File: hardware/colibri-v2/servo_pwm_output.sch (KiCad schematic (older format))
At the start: 20 parts

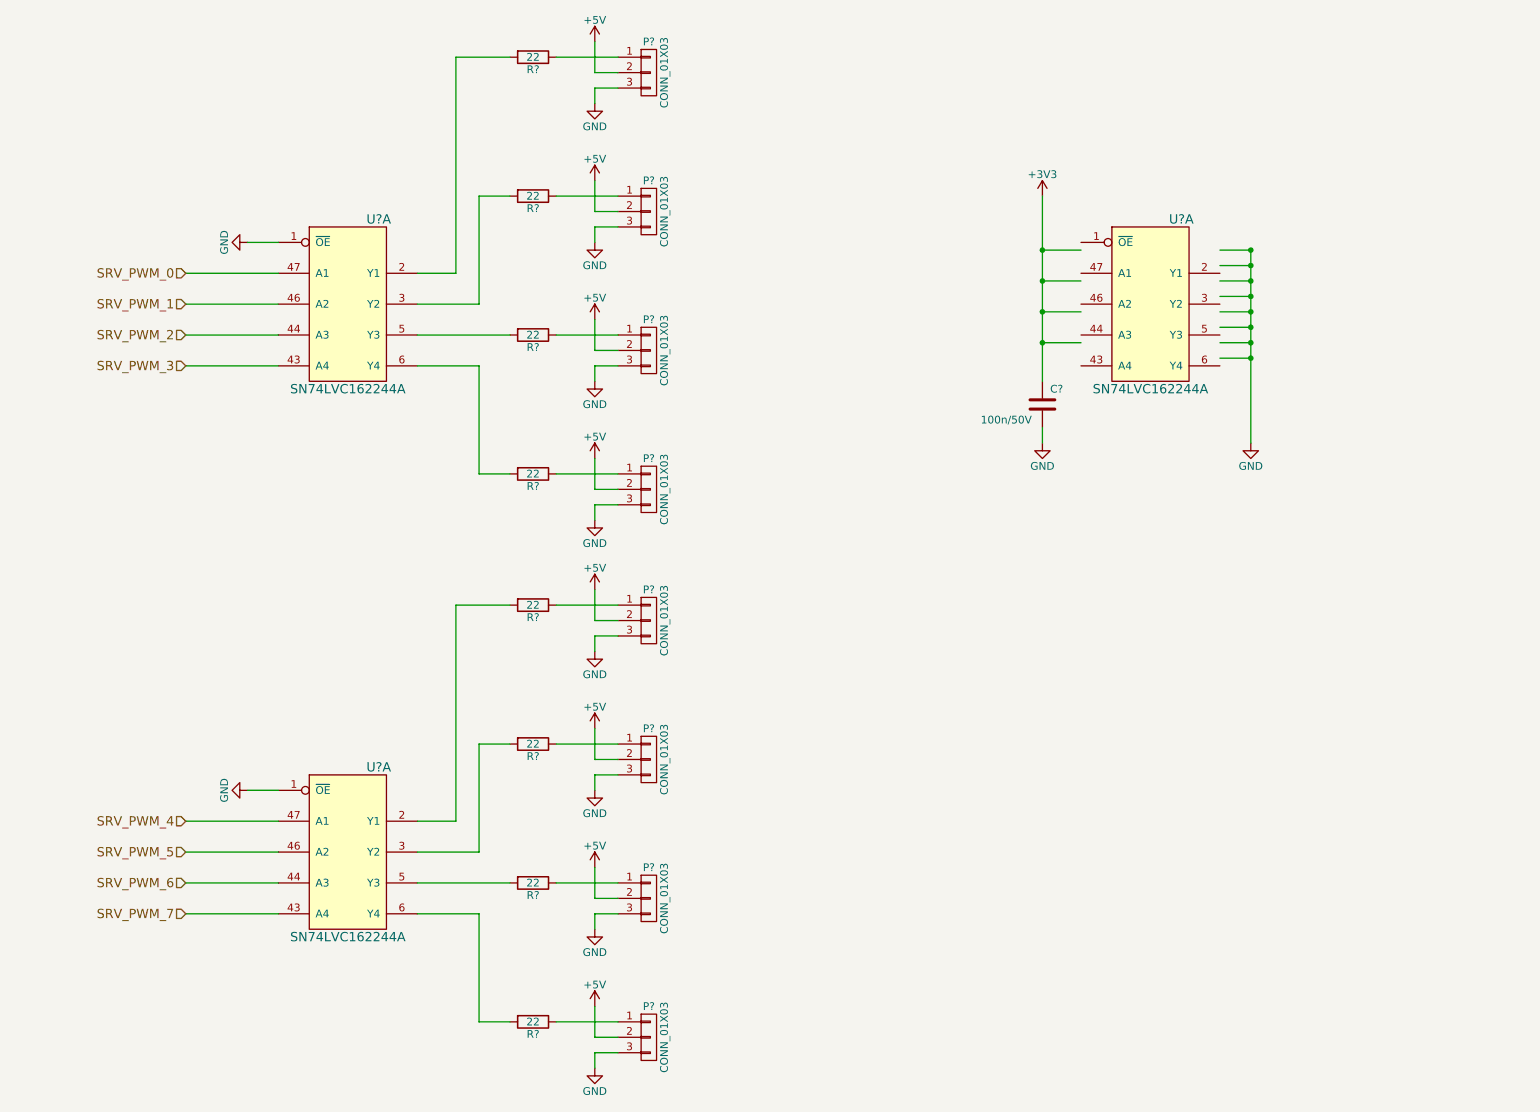
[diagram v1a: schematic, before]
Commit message: Work on wandboard lcd and usb
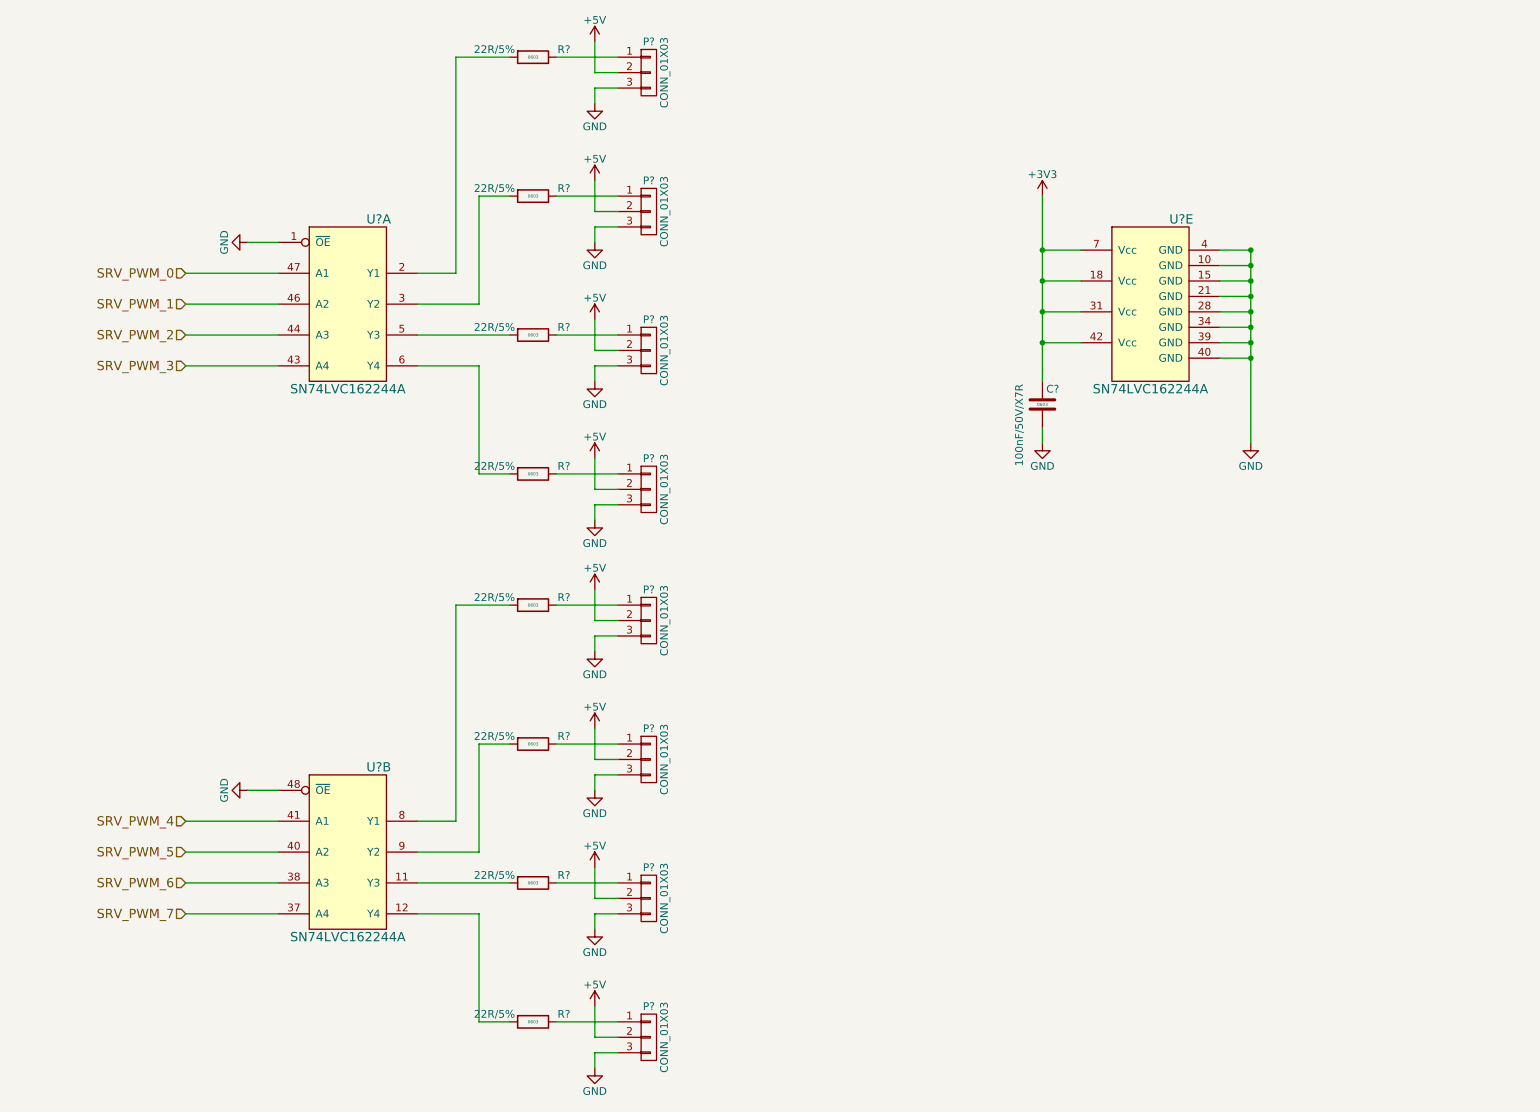
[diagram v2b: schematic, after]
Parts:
- removed C?: 100n/50V, symbol C
- removed R? (x8): 22, Resistors_SMD:R_0603, symbol R
- added C?: 100nF/50V/X7R, Capacitors_SMD:C_0603, symbol C_SMT
- added R? (x8): 22R/5%, Resistors_SMD:R_0603, symbol R_SMT
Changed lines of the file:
@@
 	1    0    0    -1
-$EndComp
-$Comp
-L R R?
-U 1 1 5619166B
-P 4300 4450
-F 0 "R?" V 4380 4450 50  0000 C CNN
-F 1 "22" V 4300 4450 50  0000 C CNN
-F 2 "Resistors_SMD:R_0603" V 4230 4450 30  0001 C CNN
-F 3 "" H 4300 4450 30  0000 C CNN
-	1    4300 4450
-	0    1    1    0
 $EndComp
 Text HLabel 2050 5850 0    60   Input ~ 0
@@
 	1    0    0    -1
 $EndComp
-$Comp
-L R R?
-U 1 1 56191934
-P 4300 5350
-F 0 "R?" V 4380 5350 50  0000 C CNN
-F 1 "22" V 4300 5350 50  0000 C CNN
-F 2 "Resistors_SMD:R_0603" V 4230 5350 30  0001 C CNN
-F 3 "" H 4300 5350 30  0000 C CNN
-	1    4300 5350
-	0    1    1    0
-$EndComp
 Text HLabel 2050 6050 0    60   Input ~ 0
 SRV_PWM_5
@@
 	1    0    0    -1
 $EndComp
-$Comp
-L R R?
-U 1 1 56191B34
-P 4300 6250
-F 0 "R?" V 4380 6250 50  0000 C CNN
-F 1 "22" V 4300 6250 50  0000 C CNN
-F 2 "Resistors_SMD:R_0603" V 4230 6250 30  0001 C CNN
-F 3 "" H 4300 6250 30  0000 C CNN
-	1    4300 6250
-	0    1    1    0
-$EndComp
 Text HLabel 2050 6250 0    60   Input ~ 0
 SRV_PWM_6
@@
 	1    0    0    -1
 $EndComp
-$Comp
-L R R?
-U 1 1 56191CF8
-P 4300 7150
-F 0 "R?" V 4380 7150 50  0000 C CNN
-F 1 "22" V 4300 7150 50  0000 C CNN
-F 2 "Resistors_SMD:R_0603" V 4230 7150 30  0001 C CNN
-F 3 "" H 4300 7150 30  0000 C CNN
-	1    4300 7150
-	0    1    1    0
-$EndComp
 Text HLabel 2050 6450 0    60   Input ~ 0
 SRV_PWM_7
@@
 	1    0    0    -1
 $EndComp
-$Comp
-L R R?
-U 1 1 5619340F
-P 4300 900
-F 0 "R?" V 4380 900 50  0000 C CNN
-F 1 "22" V 4300 900 50  0000 C CNN
-F 2 "Resistors_SMD:R_0603" V 4230 900 30  0001 C CNN
-F 3 "" H 4300 900 30  0000 C CNN
-	1    4300 900
-	0    1    1    0
-$EndComp
 Text HLabel 2050 2300 0    60   Input ~ 0
 SRV_PWM_0
@@
 	1    0    0    -1
 $EndComp
-$Comp
-L R R?
-U 1 1 56193435
-P 4300 1800
-F 0 "R?" V 4380 1800 50  0000 C CNN
-F 1 "22" V 4300 1800 50  0000 C CNN
-F 2 "Resistors_SMD:R_0603" V 4230 1800 30  0001 C CNN
-F 3 "" H 4300 1800 30  0000 C CNN
-	1    4300 1800
-	0    1    1    0
-$EndComp
 Text HLabel 2050 2500 0    60   Input ~ 0
 SRV_PWM_1
@@
 	1    0    0    -1
 $EndComp
-$Comp
-L R R?
-U 1 1 5619345B
-P 4300 2700
-F 0 "R?" V 4380 2700 50  0000 C CNN
-F 1 "22" V 4300 2700 50  0000 C CNN
-F 2 "Resistors_SMD:R_0603" V 4230 2700 30  0001 C CNN
-F 3 "" H 4300 2700 30  0000 C CNN
-	1    4300 2700
-	0    1    1    0
-$EndComp
 Text HLabel 2050 2700 0    60   Input ~ 0
 SRV_PWM_2
@@
 	1    0    0    -1
 $EndComp
-$Comp
-L R R?
-U 1 1 56193481
-P 4300 3600
-F 0 "R?" V 4380 3600 50  0000 C CNN
-F 1 "22" V 4300 3600 50  0000 C CNN
-F 2 "Resistors_SMD:R_0603" V 4230 3600 30  0001 C CNN
-F 3 "" H 4300 3600 30  0000 C CNN
-	1    4300 3600
-	0    1    1    0
-$EndComp
 Text HLabel 2050 2900 0    60   Input ~ 0
 SRV_PWM_3
@@
 $EndComp
 $Comp
-L C C?
-U 1 1 5619436E
-P 7600 3150
-F 0 "C?" H 7650 3250 50  0000 L CNN
-F 1 "100n/50V" H 7200 3050 50  0000 L CNN
-F 2 "" H 7638 3000 30  0001 C CNN
-F 3 "" H 7600 3150 60  0000 C CNN
-	1    7600 3150
-	1    0    0    -1
-$EndComp
-$Comp
 L SN74LVC162244A U?
 U 1 1 56245EEA
@@
 $Comp
 L SN74LVC162244A U?
-U 1 1 5624684B
+U 2 1 5624684B
 P 3100 6050
 F 0 "U?" H 3300 6600 60  0000 C CNN
@@
 F 2 "" H 3100 5900 60  0001 C CNN
 F 3 "" H 3100 5900 60  0000 C CNN
-	1    3100 6050
+	2    3100 6050
 	1    0    0    -1
 $EndComp
 $Comp
 L SN74LVC162244A U?
-U 1 1 562469AD
+U 5 1 562469AD
 P 8300 2500
 F 0 "U?" H 8500 3050 60  0000 C CNN
@@
 F 2 "" H 8300 2350 60  0001 C CNN
 F 3 "" H 8300 2350 60  0000 C CNN
-	1    8300 2500
+	5    8300 2500
 	1    0    0    -1
 $EndComp
@@
 Wire Wire Line
 	2450 2100 2650 2100
+$Comp
+L R_SMT R?
+U 1 1 5633B5FF
+P 4300 900
+F 0 "R?" V 4250 1100 50  0000 C CNN
+F 1 "22R/5%" V 4250 650 50  0000 C CNN
+F 2 "Resistors_SMD:R_0603" V 4450 900 30  0001 C CNN
+F 3 "" V 4380 900 30  0000 C CNN
+F 4 "0603" V 4300 900 20  0000 C CNN "SMT"
+F 5 "9331891" V 4500 900 30  0001 C CNN "Part"
+F 6 "Farnell" V 4550 900 30  0001 C CNN "Provider"
+	1    4300 900
+	0    1    1    0
+$EndComp
+$Comp
+L R_SMT R?
+U 1 1 5633B8B4
+P 4300 1800
+F 0 "R?" V 4250 2000 50  0000 C CNN
+F 1 "22R/5%" V 4250 1550 50  0000 C CNN
+F 2 "Resistors_SMD:R_0603" V 4450 1800 30  0001 C CNN
+F 3 "" V 4380 1800 30  0000 C CNN
+F 4 "0603" V 4300 1800 20  0000 C CNN "SMT"
+F 5 "9331891" V 4500 1800 30  0001 C CNN "Part"
+F 6 "Farnell" V 4550 1800 30  0001 C CNN "Provider"
+	1    4300 1800
+	0    1    1    0
+$EndComp
+$Comp
+L R_SMT R?
+U 1 1 5633B992
+P 4300 2700
+F 0 "R?" V 4250 2900 50  0000 C CNN
+F 1 "22R/5%" V 4250 2450 50  0000 C CNN
+F 2 "Resistors_SMD:R_0603" V 4450 2700 30  0001 C CNN
+F 3 "" V 4380 2700 30  0000 C CNN
+F 4 "0603" V 4300 2700 20  0000 C CNN "SMT"
+F 5 "9331891" V 4500 2700 30  0001 C CNN "Part"
+F 6 "Farnell" V 4550 2700 30  0001 C CNN "Provider"
+	1    4300 2700
+	0    1    1    0
+$EndComp
+$Comp
+L R_SMT R?
+U 1 1 5633B9F5
+P 4300 3600
+F 0 "R?" V 4250 3800 50  0000 C CNN
+F 1 "22R/5%" V 4250 3350 50  0000 C CNN
+F 2 "Resistors_SMD:R_0603" V 4450 3600 30  0001 C CNN
+F 3 "" V 4380 3600 30  0000 C CNN
+F 4 "0603" V 4300 3600 20  0000 C CNN "SMT"
+F 5 "9331891" V 4500 3600 30  0001 C CNN "Part"
+F 6 "Farnell" V 4550 3600 30  0001 C CNN "Provider"
+	1    4300 3600
+	0    1    1    0
+$EndComp
+$Comp
+L R_SMT R?
+U 1 1 5633BAF5
+P 4300 4450
+F 0 "R?" V 4250 4650 50  0000 C CNN
+F 1 "22R/5%" V 4250 4200 50  0000 C CNN
+F 2 "Resistors_SMD:R_0603" V 4450 4450 30  0001 C CNN
+F 3 "" V 4380 4450 30  0000 C CNN
+F 4 "0603" V 4300 4450 20  0000 C CNN "SMT"
+F 5 "9331891" V 4500 4450 30  0001 C CNN "Part"
+F 6 "Farnell" V 4550 4450 30  0001 C CNN "Provider"
+	1    4300 4450
+	0    1    1    0
+$EndComp
+$Comp
+L R_SMT R?
+U 1 1 5633BB80
+P 4300 5350
+F 0 "R?" V 4250 5550 50  0000 C CNN
+F 1 "22R/5%" V 4250 5100 50  0000 C CNN
+F 2 "Resistors_SMD:R_0603" V 4450 5350 30  0001 C CNN
+F 3 "" V 4380 5350 30  0000 C CNN
+F 4 "0603" V 4300 5350 20  0000 C CNN "SMT"
+F 5 "9331891" V 4500 5350 30  0001 C CNN "Part"
+F 6 "Farnell" V 4550 5350 30  0001 C CNN "Provider"
+	1    4300 5350
+	0    1    1    0
+$EndComp
+$Comp
+L R_SMT R?
+U 1 1 5633BBE8
+P 4300 6250
+F 0 "R?" V 4250 6450 50  0000 C CNN
+F 1 "22R/5%" V 4250 6000 50  0000 C CNN
+F 2 "Resistors_SMD:R_0603" V 4450 6250 30  0001 C CNN
+F 3 "" V 4380 6250 30  0000 C CNN
+F 4 "0603" V 4300 6250 20  0000 C CNN "SMT"
+F 5 "9331891" V 4500 6250 30  0001 C CNN "Part"
+F 6 "Farnell" V 4550 6250 30  0001 C CNN "Provider"
+	1    4300 6250
+	0    1    1    0
+$EndComp
+$Comp
+L R_SMT R?
+U 1 1 5633BC6F
+P 4300 7150
+F 0 "R?" V 4250 7350 50  0000 C CNN
+F 1 "22R/5%" V 4250 6900 50  0000 C CNN
+F 2 "Resistors_SMD:R_0603" V 4450 7150 30  0001 C CNN
+F 3 "" V 4380 7150 30  0000 C CNN
+F 4 "0603" V 4300 7150 20  0000 C CNN "SMT"
+F 5 "9331891" V 4500 7150 30  0001 C CNN "Part"
+F 6 "Farnell" V 4550 7150 30  0001 C CNN "Provider"
+	1    4300 7150
+	0    1    1    0
+$EndComp
+$Comp
+L C_SMT C?
+U 1 1 5633CB48
+P 7600 3150
+F 0 "C?" H 7625 3250 50  0000 L CNN
+F 1 "100nF/50V/X7R" V 7450 2750 50  0000 L CNN
+F 2 "Capacitors_SMD:C_0603" H 7630 3000 30  0001 L CNN
+F 3 "" H 7625 3250 60  0000 L CNN
+F 4 "0603" H 7600 3150 20  0000 C CNN "SMT"
+F 5 "1414028" H 7630 2960 30  0001 L CNN "Part"
+F 6 "Farnell" H 7630 2920 30  0001 L CNN "Provider"
+	1    7600 3150
+	1    0    0    -1
+$EndComp
 $EndSCHEMATC

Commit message: Work on PWM, USB, MEMS, Power
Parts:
- removed R? (x8): 22R/5%, Resistors_SMD:R_0603, symbol R_SMT
- added R?: 10K/5%, Resistors_SMD:R_0603, symbol R_SMT
- added R?: 0R, Resistors_SMD:R_0603, symbol R_SMT
- added R?: NA, Resistors_SMD:R_0603, symbol R_SMT
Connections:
- net +3V3: now also R?.1
- net GND: now also R?.1; no longer U?.1 (~OE), U?.48 (~OE)
- net at P?.1 (P1): now also U?.8 (Y1)
- net at P?.1 (P1): now also U?.9 (Y2)
- net at P?.1 (P1): now also U?.11 (Y3)
- net at P?.1 (P1): now also U?.12 (Y4)
- net at P?.1 (P1): now also U?.2 (Y1)
- net at P?.1 (P1): now also U?.3 (Y2)
- net at P?.1 (P1): now also U?.5 (Y3)
- net at P?.1 (P1): now also U?.6 (Y4)
- new net PWM_SRV_ENABLE: R?.2
- new net SRV_OE: R?.1, R?.2, R?.2, U?.1 (~OE), U?.48 (~OE)
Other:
- moved on the sheet: P?, U?A, U?B

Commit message: Work on power conrol sheet
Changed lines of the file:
@@
 Connection ~ 8950 2850
 Wire Wire Line
-	8950 2150 8950 2250
-Wire Wire Line
-	8950 2250 8950 2350
-Wire Wire Line
-	8950 2350 8950 2450
-Wire Wire Line
-	8950 2450 8950 2550
-Wire Wire Line
-	8950 2550 8950 2650
-Wire Wire Line
-	8950 2650 8950 2750
-Wire Wire Line
-	8950 2750 8950 2850
-Wire Wire Line
-	8950 2850 8950 3400
+	8950 2150 8950 3400
 Wire Wire Line
 	7600 2350 7850 2350
@@
 Connection ~ 7600 2150
 Wire Wire Line
-	7600 1800 7600 2150
-Wire Wire Line
-	7600 2150 7600 2350
-Wire Wire Line
-	7600 2350 7600 2550
-Wire Wire Line
-	7600 2550 7600 2750
-Wire Wire Line
-	7600 2750 7600 3000
+	7600 1800 7600 3000
 Wire Wire Line
 	7850 2550 7600 2550
@@
 	1900 4400 2050 4400
 Wire Wire Line
-	2350 4400 2600 4400
-Wire Wire Line
-	2600 4400 3400 4400
+	2350 4400 3400 4400
 $Comp
 L R_SMT R?
@@
 $EndComp
 Wire Wire Line
-	2600 4200 2600 4400
-Wire Wire Line
-	2600 4400 2600 4600
+	2600 4200 2600 4600
 Connection ~ 2600 4400
 Wire Wire Line
